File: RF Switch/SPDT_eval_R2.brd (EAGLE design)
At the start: 23.9 x 26.4 mm, 10 parts, among them J4 22-23-2051, U1 QPC1022

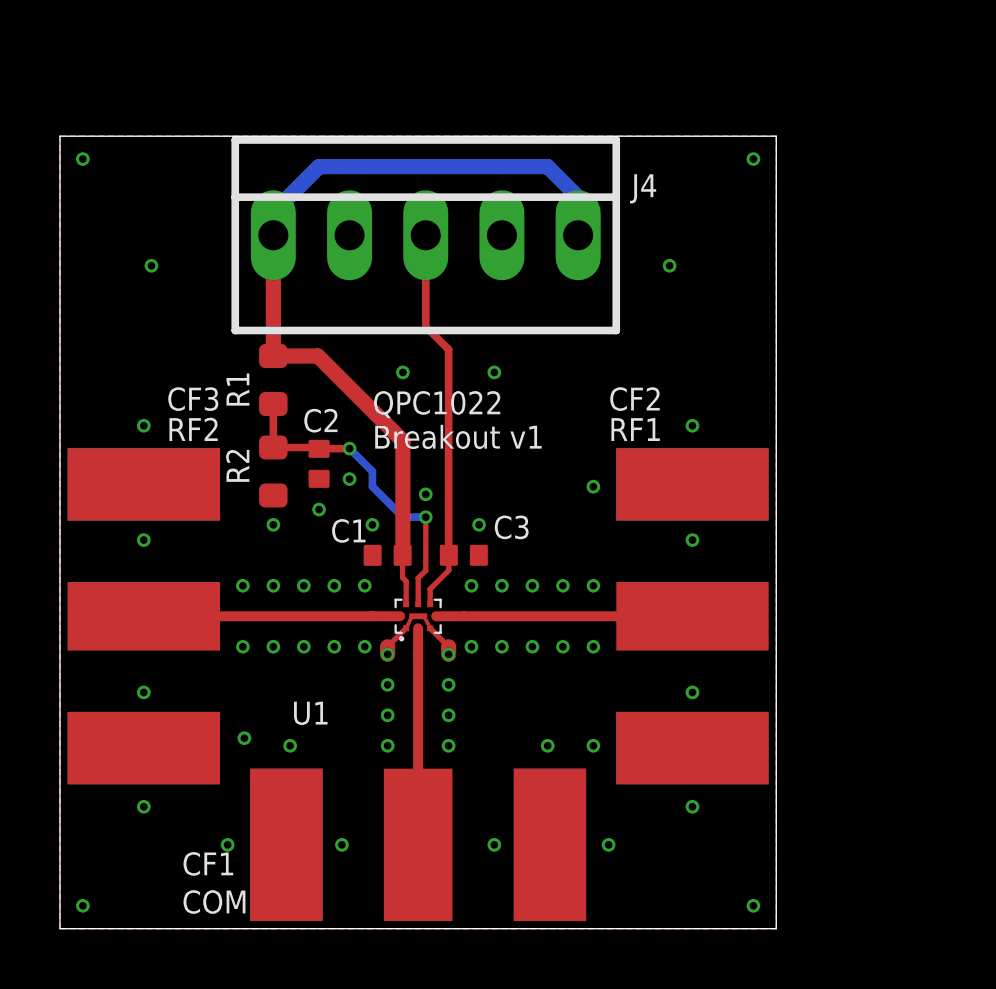
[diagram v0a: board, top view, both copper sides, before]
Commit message: Added mounting holes, cleaned up text a bit.
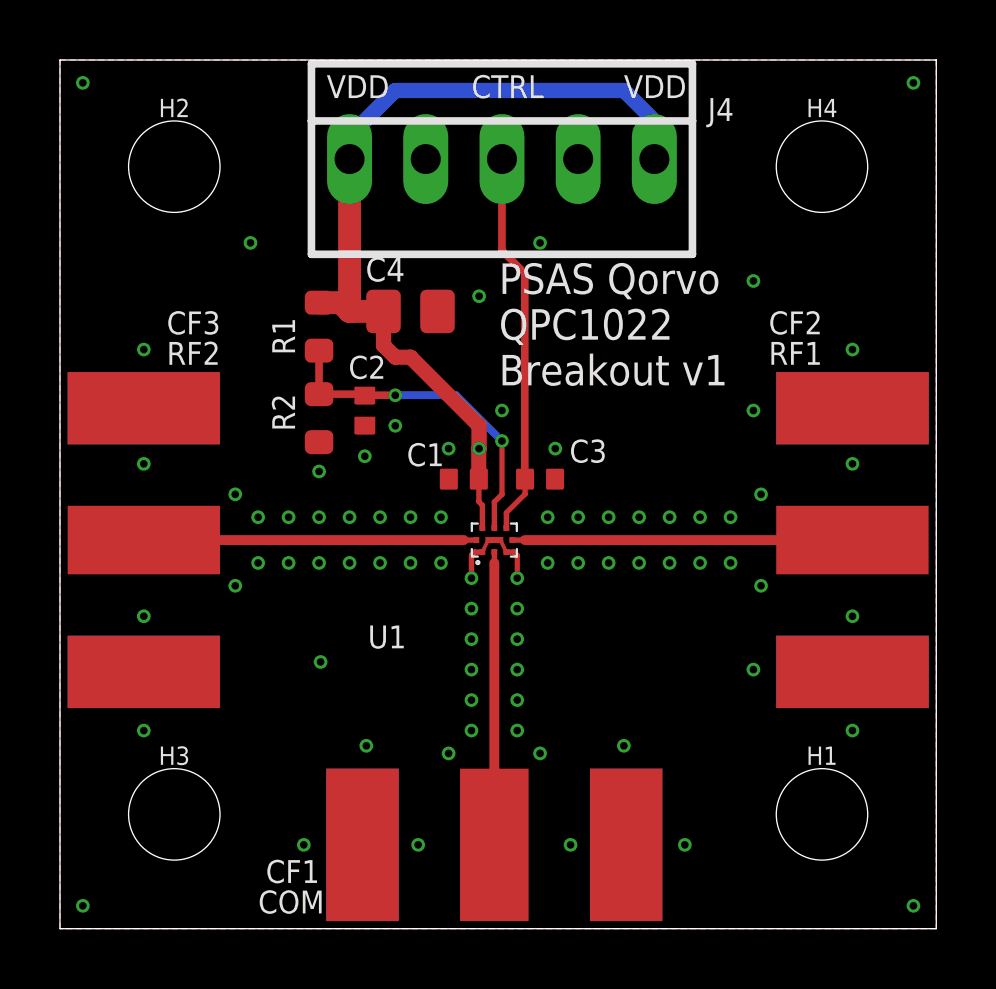
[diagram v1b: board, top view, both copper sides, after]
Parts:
- added C4: 10u, rcl_custom:.0805-B-NOSILK
- added H1, H2, H3, H4: STAND-OFFTIGHT, SparkFun-Hardware:STAND-OFF-TIGHT
- C1: value 2.2n -> 100n
- moved CF2 5.91 mm to (26.4, 13.0)
- moved C1 3.59 mm to (13.5, 15.0)
- moved C3 3.59 mm to (16.0, 15.0)
- moved U1 3.59 mm to (14.5, 13.0)
- moved J4 3.59 mm to (14.7, 25.7)
- moved CF3 2.54 mm to (2.79, 13.0)
- moved CF1 2.54 mm to (14.5, 2.79)
- moved C2 2.34 mm to (10.2, 17.3)
- moved R2 2.34 mm to (8.64, 17.0)
- moved R1 2.34 mm to (8.64, 20.1)
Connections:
- net GND: now also C4.2
- net VDD: now also C4.1
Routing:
- net RF1: track 8.54 -> 11.3 mm
- net RF2: track 8.54 -> 11.1 mm
- net COM: track 7.22 -> 9.76 mm
- net VDD: track 28.3 -> 29.5 mm, vias 0 -> 1
- net GND: track 3.55 -> 3.64 mm, vias 59 -> 77
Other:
- board size 23.9 x 26.4 mm -> 29.2 x 29 mm
- board text added: "CTRL"
- board text added: "PSAS Qorvo QPC1022 Breakout v1"
- board text added: "VDD"
- board text removed: "QPC1022 Breakout v1"
